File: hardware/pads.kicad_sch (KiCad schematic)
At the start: 22 parts, among them J10 M3, J13 M4, J20 LED, J21 5V, J22 BZ-, J23 CAM, J24 5V, J25 GND, J26 VHD, J27 GND, J28 TX0, J29 RX0, J31 USB, J32 CAM, J33 GND, J34 SM06B-SRSS-TB(LF)(SN), J4 M1, J7 M2

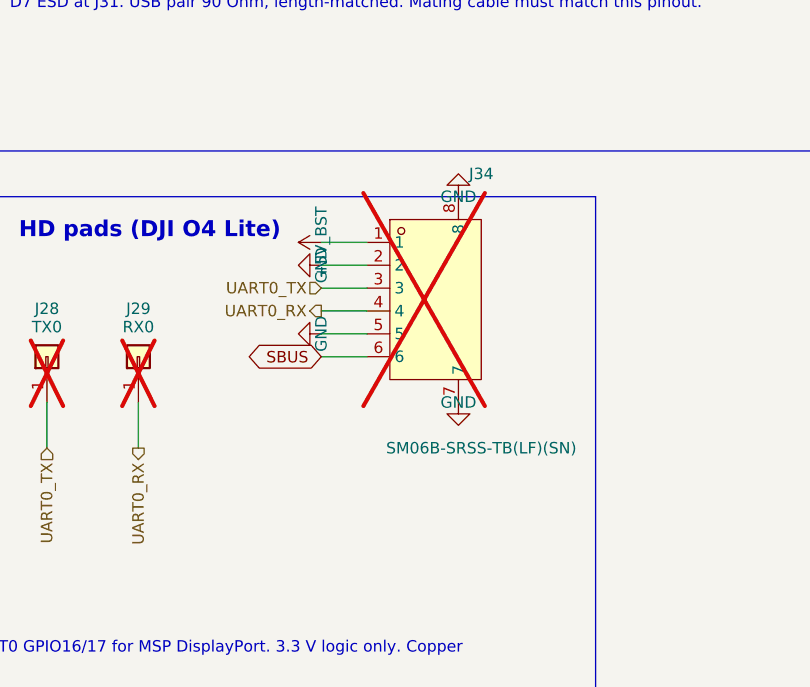
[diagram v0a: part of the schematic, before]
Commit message: Drop the HD plug; keep pads J26-J29 plus an SBUS pad J34 on GPIO29 (D127)
The JST SH 6-pin (about 49 mm2) does not fit. J34 is now a 1.0 x 1.2 mm
SBUS pad beside the HD pads. Removes the plug, its project lib symbol and
footprint. Netlist vs 938d711: only J34 (SBUS) and U10 pin 43 change; ERC 21.

Co-Authored-By: Claude Opus 5.5 <noreply@anthropic.com>
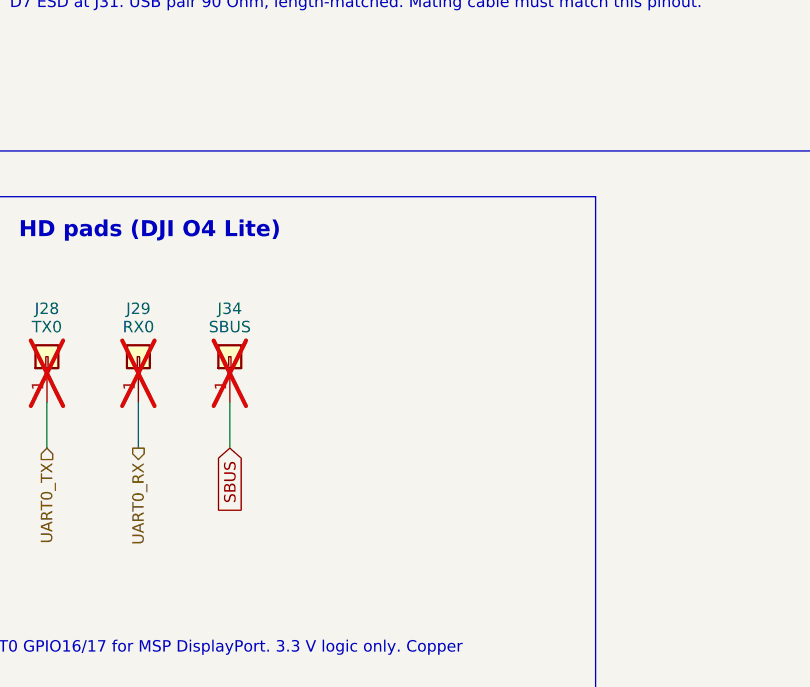
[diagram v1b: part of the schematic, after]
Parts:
- removed J34: SM06B-SRSS-TB(LF)(SN), lib:CONN-SMD_SM06B-SRSS-TB-LF-SN, symbol lib:SM06B-SRSS-TB(LF)(SN)
- added J34: SBUS, lib:SolderPad_1.0x1.2mm, symbol lib:SolderPad_01x01
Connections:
- net SBUS: now also J34.1 (Pin_1)

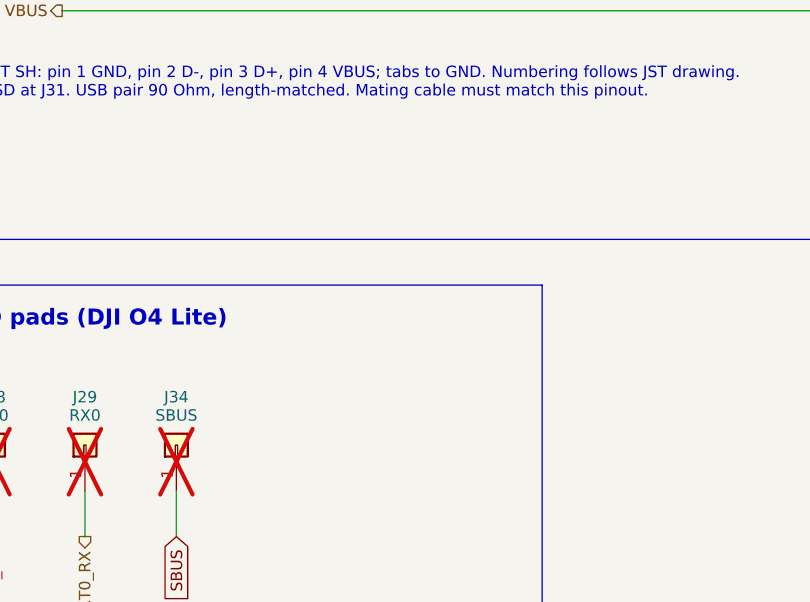
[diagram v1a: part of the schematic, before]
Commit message: HD VTX plug J35: JST SH 4-pin side entry in parallel with J26-J29 (D128)
SM04B-SRSS-TB(LF)(SN), LCSC C160404, 1 A per contact; symbol copied into
the project lib from the OpenDrone part (pins passive), footprint already
local. Netlist: only J35 pins change (+5V_BST, GND, UART0_TX, UART0_RX,
mounting GND); ERC unchanged (21).

Co-Authored-By: Claude Opus 5.5 <noreply@anthropic.com>
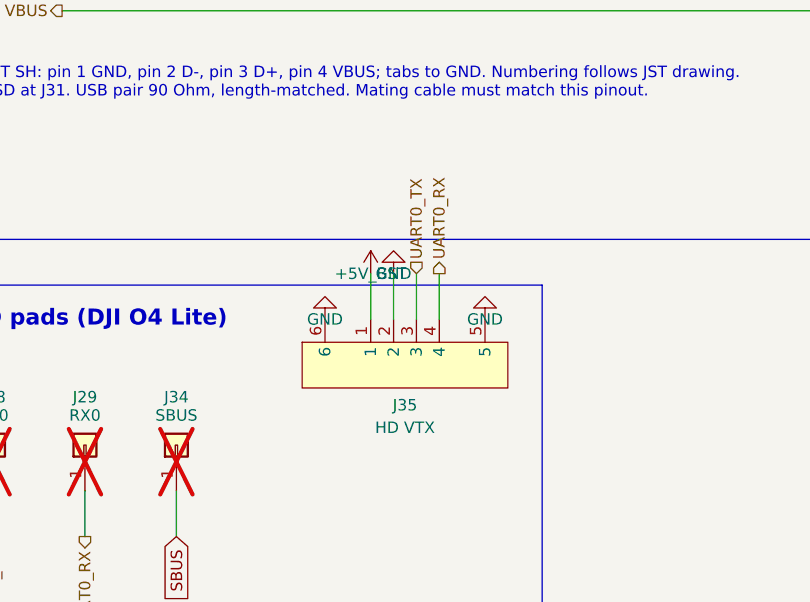
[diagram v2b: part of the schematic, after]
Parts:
- added J35: HD VTX, lib:CONN-SMD_4P-P1.00_SM04B-SRSS-TB-LF-SN, symbol lib:SM04B-SRSS-TB
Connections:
- net +5V_BST: now also J35.1
- net GND: now also J35.2, J35.5, J35.6
- net UART0_RX: now also J35.4
- net UART0_TX: now also J35.3

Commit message: Owner routing, per-ESC 22uF bulk caps, J34 removed (WIP save, unreviewed)
Co-Authored-By: Claude Opus 5.5 <noreply@anthropic.com>
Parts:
- removed J34: SBUS, lib:SolderPad_1.0x1.2mm, symbol lib:SolderPad_01x01
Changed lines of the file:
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@@
-	(wire
-		(pts
-			(xy 279.4 121.92) (xy 279.4 127)
-		)
-		(stroke
-			(width 0)
-			(type default)
-		)
-	)
 	(wire
 		(pts
@@
 			(width 0)
 			(type default)
-		)
-	)
-	(global_label "SBUS"
-		(shape input)
-		(at 279.4 127 270)
-		(fields_autoplaced yes)
-		(effects
-			(font
-				(size 1.27 1.27)
-			)
-			(justify right)
-		)
-		(property "Intersheetrefs" "${INTERSHEET_REFS}"
-			(at 279.4 127 0)
-			(hide yes)
-			(show_name no)
-			(do_not_autoplace no)
-			(effects
-				(font
-					(size 1.27 1.27)
-				)
-				(justify right)
-			)
 		)
 	)
@@
 					(unit 1)
 				)
-			)
-		)
-	)
-	(symbol
-		(lib_id "lib:SolderPad_01x01")
-		(at 279.4 116.84 90)
-		(unit 1)
-		(body_style 1)
-		(exclude_from_sim no)
-		(in_bom no)
-		(on_board yes)
-		(in_pos_files no)
-		(dnp yes)
-		(property "Reference" "J34"
-			(at 279.4 111.506 90)
-			(show_name no)
-			(do_not_autoplace no)
-			(effects
-				(font
-					(size 1.27 1.27)
-				)
-			)
-		)
-		(property "Value" "SBUS"
-			(at 279.4 113.538 90)
-			(show_name no)
-			(do_not_autoplace no)
-			(effects
-				(font
-					(size 1.27 1.27)
-				)
-			)
-		)
-		(property "Footprint" "lib:SolderPad_1.0x1.2mm"
-			(at 279.4 116.84 0)
-			(hide yes)
-			(show_name no)
-			(do_not_autoplace no)
-			(effects
-				(font
-					(size 1.27 1.27)
-				)
-			)
-		)
-		(property "Datasheet" ""
-			(at 279.4 116.84 0)
-			(hide yes)
-			(show_name no)
-			(do_not_autoplace no)
-			(effects
-				(font
-					(size 1.27 1.27)
-				)
-			)
-		)
-		(property "Description" "Solder pad (one bare copper land, no part fitted): Connector_Generic:Conn_01x01 graphics with filters for the project SolderPad_* / BattPad_* footprints (LINEUP-CONVENTIONS rule 16)"
-			(at 279.4 116.84 0)
-			(hide yes)
-			(show_name no)
-			(do_not_autoplace no)
-			(effects
-				(font
-					(size 1.27 1.27)
-				)
-			)
-		)
-		(pin "1"
-		)
-		(instances
-			(project "OpenAIO-Whoop"
-				(path "/2c3a7206-1e66-4d43-a02f-491225e20dd6/8d214749-72cf-5803-99b7-260f0c3f1838"
-					(reference "J34")
-					(unit 1)
-				)

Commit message: Every schematic symbol project-local (Device, power, Connector, Mechanical moved into lib)
tools/localise_symbols.py from OpenAIO. Netlist identical, ERC unchanged (0 errors, 24 warnings), every symbol, footprint and 3D model resolves inside the repo.

Co-Authored-By: Claude Opus 5.5 <noreply@anthropic.com>
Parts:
- H1, H2, H3: symbol Mechanical:MountingHole -> lib:MountingHole
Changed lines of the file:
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@@
 	)
 	(symbol
-		(lib_id "power:GND")
+		(lib_id "lib:GND")
 		(at 30.48 127 0)
 		(unit 1)
@@
 	)
 	(symbol
-		(lib_id "Mechanical:MountingHole")
+		(lib_id "lib:MountingHole")
 		(at 81.28 196.85 0)
 		(unit 1)
@@
 	)
 	(symbol
-		(lib_id "Mechanical:MountingHole")
+		(lib_id "lib:MountingHole")
 		(at 55.88 196.85 0)
 		(unit 1)
@@
 	)
 	(symbol
-		(lib_id "power:GND")
+		(lib_id "lib:GND")
 		(at 367.03 43.18 0)
 		(unit 1)
@@
 	)
 	(symbol
-		(lib_id "Mechanical:MountingHole")
+		(lib_id "lib:MountingHole")
 		(at 30.48 196.85 0)
 		(unit 1)
@@
 	)
 	(symbol
-		(lib_id "power:GND")
+		(lib_id "lib:GND")
 		(at 167.64 127 0)
 		(unit 1)
@@
 	)
 	(symbol
-		(lib_id "power:GND")
+		(lib_id "lib:GND")
 		(at 173.99 127 0)
 		(unit 1)
@@
 	)
 	(symbol
-		(lib_id "power:+5V")
+		(lib_id "lib:+5V")
 		(at 238.76 127 180)
 		(unit 1)
@@
 	)
 	(symbol
-		(lib_id "power:PWR_FLAG")
+		(lib_id "lib:PWR_FLAG")
 		(at 382.27 58.42 0)
 		(unit 1)
@@
 	)
 	(symbol
-		(lib_id "power:+5V")
+		(lib_id "lib:+5V")
 		(at 139.7 127 180)
 		(unit 1)
@@
 	)
 	(symbol
-		(lib_id "power:+5V")
+		(lib_id "lib:+5V")
 		(at 300.99 97.79 0)
 		(unit 1)
@@
 	)
 	(symbol
-		(lib_id "power:GND")
+		(lib_id "lib:GND")
 		(at 379.73 43.18 0)
 		(unit 1)
@@
 	)
 	(symbol
-		(lib_id "power:GND")
+		(lib_id "lib:GND")
 		(at 347.98 43.18 0)
 		(unit 1)
@@
 	)
 	(symbol
-		(lib_id "power:GND")
+		(lib_id "lib:GND")
 		(at 313.69 102.87 180)
 		(unit 1)
@@
 	)
 	(symbol
-		(lib_id "power:GND")
+		(lib_id "lib:GND")
 		(at 303.53 97.79 180)
 		(unit 1)
@@
 	)
 	(symbol
-		(lib_id "power:GND")
+		(lib_id "lib:GND")
 		(at 129.54 127 0)
 		(unit 1)
@@
 	)
 	(symbol
-		(lib_id "power:+5V")
+		(lib_id "lib:+5V")
 		(at 50.8 127 180)
 		(unit 1)
@@
 	)
 	(symbol
-		(lib_id "power:GND")
+		(lib_id "lib:GND")
 		(at 248.92 127 0)
 		(unit 1)
@@
 	)
 	(symbol
-		(lib_id "power:+5V")
+		(lib_id "lib:+5V")
 		(at 170.18 132.08 180)
 		(unit 1)
@@
 	)
 	(symbol
-		(lib_id "power:GND")
+		(lib_id "lib:GND")
 		(at 295.91 102.87 180)
 		(unit 1)
